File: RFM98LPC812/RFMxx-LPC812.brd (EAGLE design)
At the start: 60 x 38.7 mm, 34 parts, among them P14 TPB1,27, X1 BU-SMA-V, X2 BU-SMA-V

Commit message: cosmetic changes to board lables
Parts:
- renumbered U$1 to LPC812_RFM69, U$5 to LPC812_RFM98
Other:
- board text removed: "LPC812"

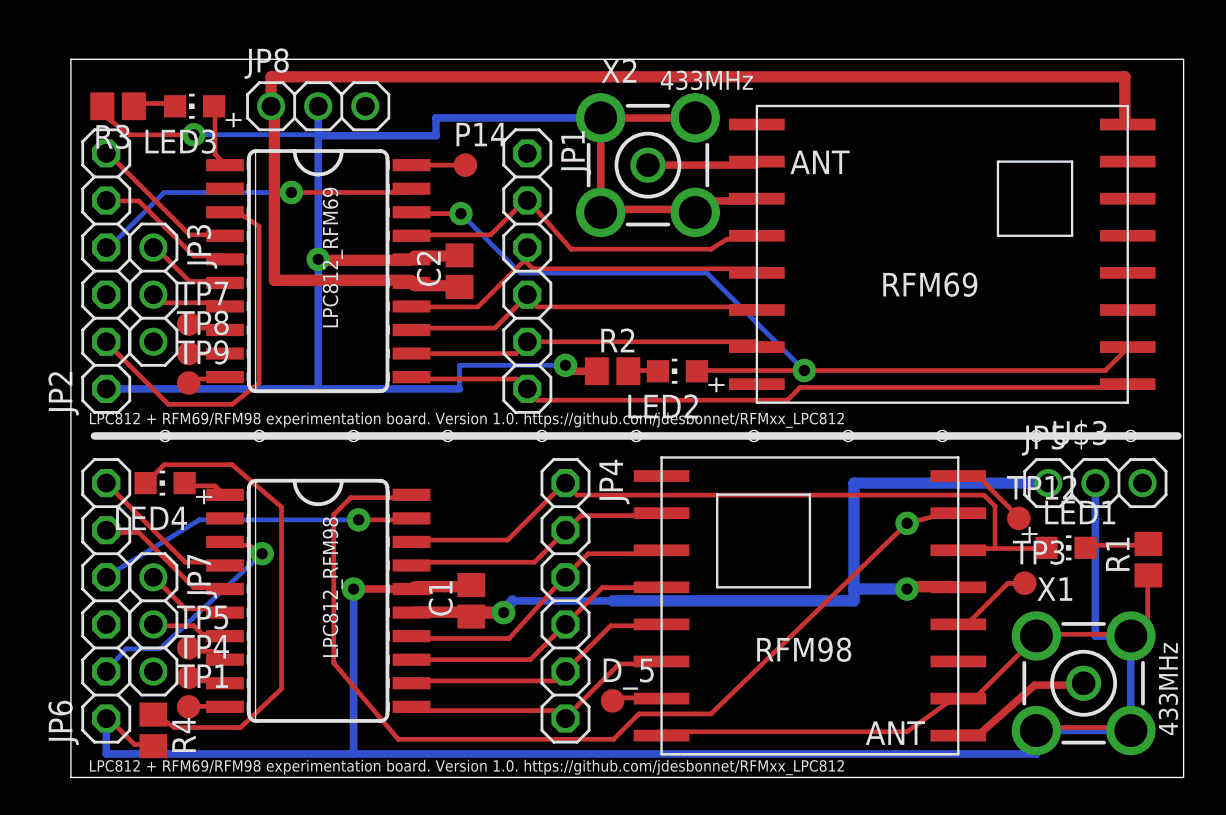
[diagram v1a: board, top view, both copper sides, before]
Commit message: label cosmetic changes
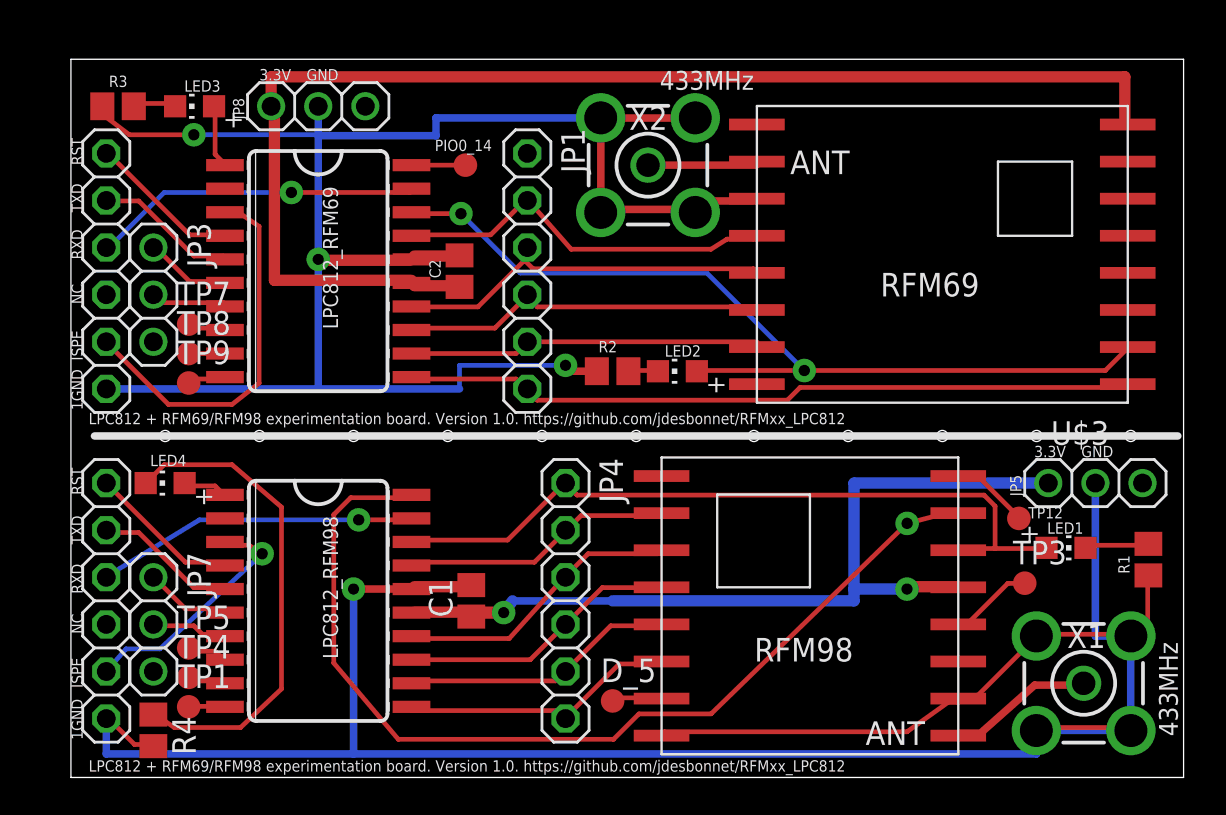
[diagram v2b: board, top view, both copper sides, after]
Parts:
- C2: value 0.1uF -> 100nF
- renumbered P14 to PIO0_14
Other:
- board text added: "1GND"
- board text added: "3.3V"
- board text added: "GND"
- board text added: "ISPE"
- board text added: "NC"
- board text added: "RST"
- board text added: "RXD"
- board text added: "TXD"

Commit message: label cosmetic changes
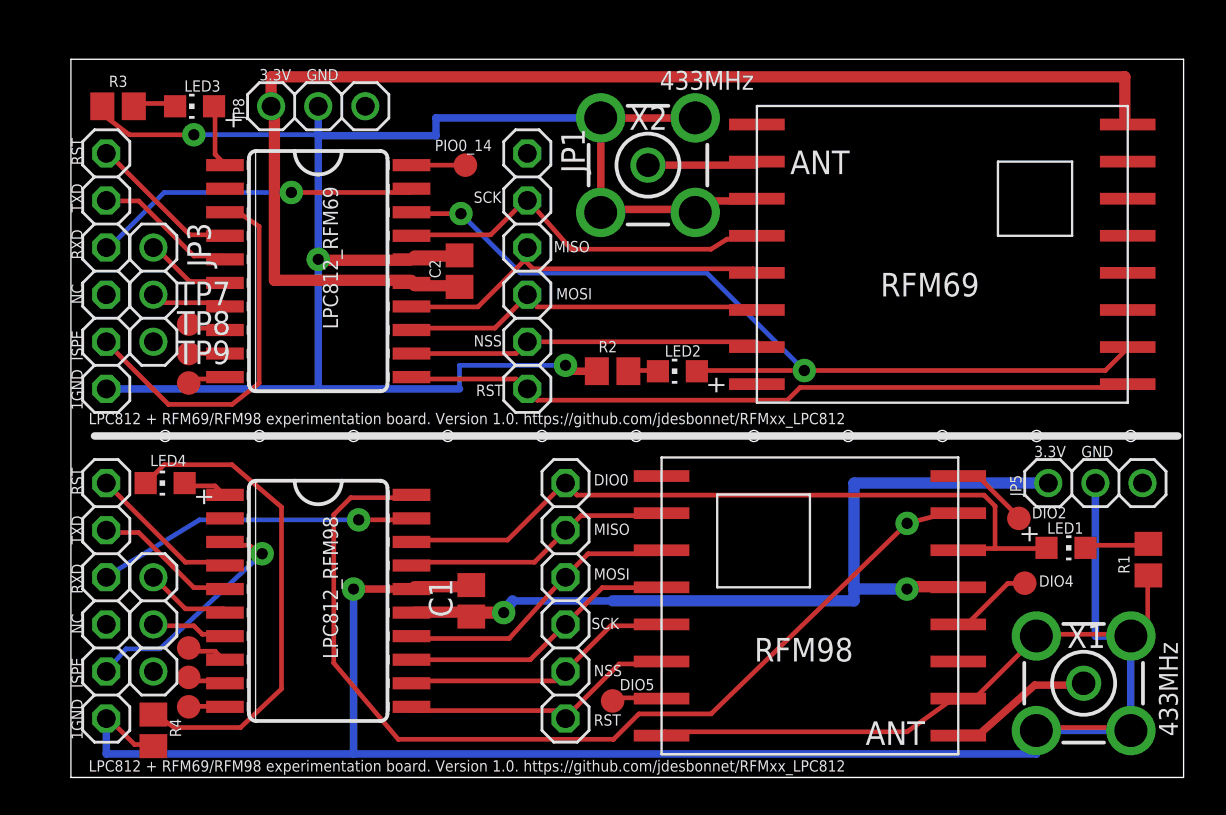
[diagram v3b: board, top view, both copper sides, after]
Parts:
- renumbered TP3 to TP3X
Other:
- board text added: "DIO0"
- board text added: "DIO2"
- board text added: "DIO4"
- board text added: "DIO5"
- board text added: "MISO"
- board text added: "MOSI"
- board text added: "NSS"
- board text added: "SCK"
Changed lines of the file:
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@@
 <text x="0.635" y="12.573" size="0.6096" layer="21" rot="R90">TXD</text>
 <text x="0.635" y="15.24" size="0.6096" layer="21" rot="R90">RST</text>
+<text x="28.194" y="2.794" size="0.6096" layer="21">RST</text>
+<text x="28.194" y="5.461" size="0.6096" layer="21">NSS</text>
+<text x="28.067" y="8.001" size="0.6096" layer="21">SCK</text>
+<text x="28.194" y="10.668" size="0.6096" layer="21">MOSI</text>
+<text x="28.194" y="13.081" size="0.6096" layer="21">MISO</text>
+<text x="28.194" y="15.748" size="0.6096" layer="21">DIO0</text>
+<text x="52.197" y="10.287" size="0.6096" layer="21">DIO4</text>
+<text x="29.591" y="4.699" size="0.6096" layer="21">DIO5</text>
+<text x="51.816" y="13.97" size="0.6096" layer="21">DIO2</text>
+<text x="21.844" y="20.574" size="0.6096" layer="21">RST</text>
+<text x="21.717" y="23.241" size="0.6096" layer="21">NSS</text>
+<text x="26.162" y="25.781" size="0.6096" layer="21">MOSI</text>
+<text x="26.035" y="28.321" size="0.6096" layer="21">MISO</text>
+<text x="21.717" y="30.988" size="0.6096" layer="21">SCK</text>
 </plain>
 <attributes>
@@
 </element>
 <element name="LPC812_RFM69" library="LPC812" package="SOIC20" value="LPC812M101JD20" x="13.335" y="26.035" rot="R270"/>
-<element name="U$3" library="hoperf-rfmxx" package="RFM69_PADS" value="RFM69HW" x="46.99" y="29.21" rot="R180"/>
+<element name="U$3" library="hoperf-rfmxx" package="RFM69_PADS" value="RFM69HW" x="46.99" y="29.21" smashed="yes" rot="R180"/>
 <element name="JP2" library="adafruit" package="1X06" value="" x="1.905" y="27.305" smashed="yes" rot="R90">
 <attribute name="VALUE" x="5.08" y="19.685" size="1.27" layer="27" rot="R90"/>
 </element>
 <element name="LPC812_RFM98" library="LPC812" package="SOIC20" value="LPC812M101JD20" x="13.335" y="8.255" rot="R270"/>
-<element name="JP4" library="adafruit" package="1X06" value="" x="26.67" y="9.525" rot="R270"/>
+<element name="JP4" library="adafruit" package="1X06" value="" x="26.67" y="9.525" smashed="yes" rot="R270">
+<attribute name="VALUE" x="23.495" y="17.145" size="1.27" layer="27" rot="R270"/>
+</element>
 <element name="JP5" library="adafruit" package="1X03" value="" x="55.245" y="15.875" smashed="yes">
 <attribute name="NAME" x="51.2572" y="15.1638" size="0.6096" layer="25" ratio="10" rot="R90"/>
@@
 <attribute name="NAME" x="20.574" y="8.636" size="1.27" layer="25" rot="R90"/>
 </element>
-<element name="TP1" library="testpad" package="B1,27" value="TPB1,27" x="6.35" y="3.81">
-<attribute name="TP_SIGNAL_NAME" value="" x="6.35" y="3.81" size="1.778" layer="27" display="off"/>
-</element>
-<element name="JP7" library="adafruit" package="1X03" value="" x="4.445" y="8.255" rot="R270"/>
-<element name="TP3" library="testpad" package="B1,27" value="TPB1,27" x="51.435" y="10.4775">
-<attribute name="TP_SIGNAL_NAME" value="" x="51.435" y="10.4775" size="1.27" layer="27" display="off"/>
-</element>
-<element name="TP4" library="testpad" package="B1,27" value="TPB1,27" x="6.35" y="5.3975">
-<attribute name="TP_SIGNAL_NAME" value="" x="6.35" y="5.3975" size="1.27" layer="27" display="off"/>
-</element>
-<element name="TP5" library="testpad" package="B1,27" value="TPB1,27" x="6.35" y="6.985">
-<attribute name="TP_SIGNAL_NAME" value="" x="6.35" y="6.985" size="1.27" layer="27" display="off"/>
-</element>
-<element name="D_5" library="testpad" package="B1,27" value="TPB1,27" x="29.21" y="4.1275">
-<attribute name="TP_SIGNAL_NAME" value="" x="29.21" y="4.1275" size="1.27" layer="27" display="off"/>
+<element name="TP1" library="testpad" package="B1,27" value="TPB1,27" x="6.35" y="3.81" smashed="yes">
+<attribute name="TP_SIGNAL_NAME" value="" x="5.715" y="1.905" size="1" layer="37"/>
+<attribute name="VALUE" x="5.715" y="3.048" size="0.0254" layer="27"/>
+</element>
+<element name="JP7" library="adafruit" package="1X03" value="" x="4.445" y="8.255" smashed="yes" rot="R270">
+<attribute name="VALUE" x="1.27" y="12.065" size="1.27" layer="27" rot="R270"/>
+</element>
+<element name="TP3X" library="testpad" package="B1,27" value="TPB1,27" x="51.435" y="10.4775" smashed="yes">
+<attribute name="TP_SIGNAL_NAME" value="" x="50.8" y="8.5725" size="1" layer="37"/>
+<attribute name="VALUE" x="50.8" y="9.7155" size="0.0254" layer="27"/>
+</element>
+<element name="TP4" library="testpad" package="B1,27" value="TPB1,27" x="6.35" y="5.3975" smashed="yes">
+<attribute name="TP_SIGNAL_NAME" value="" x="5.715" y="3.4925" size="1" layer="37"/>
+<attribute name="VALUE" x="5.715" y="4.6355" size="0.0254" layer="27"/>
+</element>
+<element name="TP5" library="testpad" package="B1,27" value="TPB1,27" x="6.35" y="6.985" smashed="yes">
+<attribute name="TP_SIGNAL_NAME" value="" x="5.715" y="5.08" size="1" layer="37"/>
+<attribute name="VALUE" x="5.715" y="6.223" size="0.0254" layer="27"/>
+</element>
+<element name="D_5" library="testpad" package="B1,27" value="TPB1,27" x="29.21" y="4.1275" smashed="yes">
+<attribute name="TP_SIGNAL_NAME" value="" x="28.575" y="2.2225" size="1" layer="37"/>
+<attribute name="VALUE" x="28.575" y="3.3655" size="0.0254" layer="27"/>
 </element>
 <element name="C2" library="adafruit" package="C0805" value="100nF" x="20.955" y="27.305" smashed="yes" rot="R90">
@@
 <attribute name="VALUE" x="6.35" y="18.415" size="1.27" layer="27" rot="R180"/>
 </element>
-<element name="R4" library="resistor" package="R0805" value="3K3" x="4.445" y="2.54" rot="R270"/>
+<element name="R4" library="resistor" package="R0805" value="3K3" x="4.445" y="2.54" smashed="yes" rot="R270">
+<attribute name="NAME" x="5.334" y="3.175" size="0.6096" layer="25" rot="R270"/>
+</element>
 <element name="TP7" library="testpad" package="B1,27" value="TPB1,27" x="6.35" y="24.4475">
 <attribute name="TP_SIGNAL_NAME" value="" x="6.35" y="24.4475" size="1.27" layer="27" display="off"/>
@@
 <element name="TP12" library="testpad" package="B1,27" value="TPB1,27" x="51.1175" y="13.97" smashed="yes">
 <attribute name="TP_SIGNAL_NAME" value="" x="50.4825" y="12.065" size="1" layer="37"/>
-<attribute name="NAME" x="51.6255" y="13.97" size="0.6096" layer="25" ratio="10"/>
 <attribute name="VALUE" x="50.4825" y="13.208" size="0.0254" layer="27"/>
 </element>
@@
 <signal name="N$31">
 <contactref element="U$2" pad="DIO4"/>
-<contactref element="TP3" pad="TP"/>
+<contactref element="TP3X" pad="TP"/>
 <wire x1="50.5206" y1="10.4648" x2="51.6636" y2="10.4648" width="0.254" layer="1"/>
 <wire x1="48.4632" y1="8.4074" x2="50.5206" y2="10.4648" width="0.254" layer="1"/>
